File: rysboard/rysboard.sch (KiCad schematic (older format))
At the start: 8 parts, among them J1 RPi4, J17 Conn_01x03

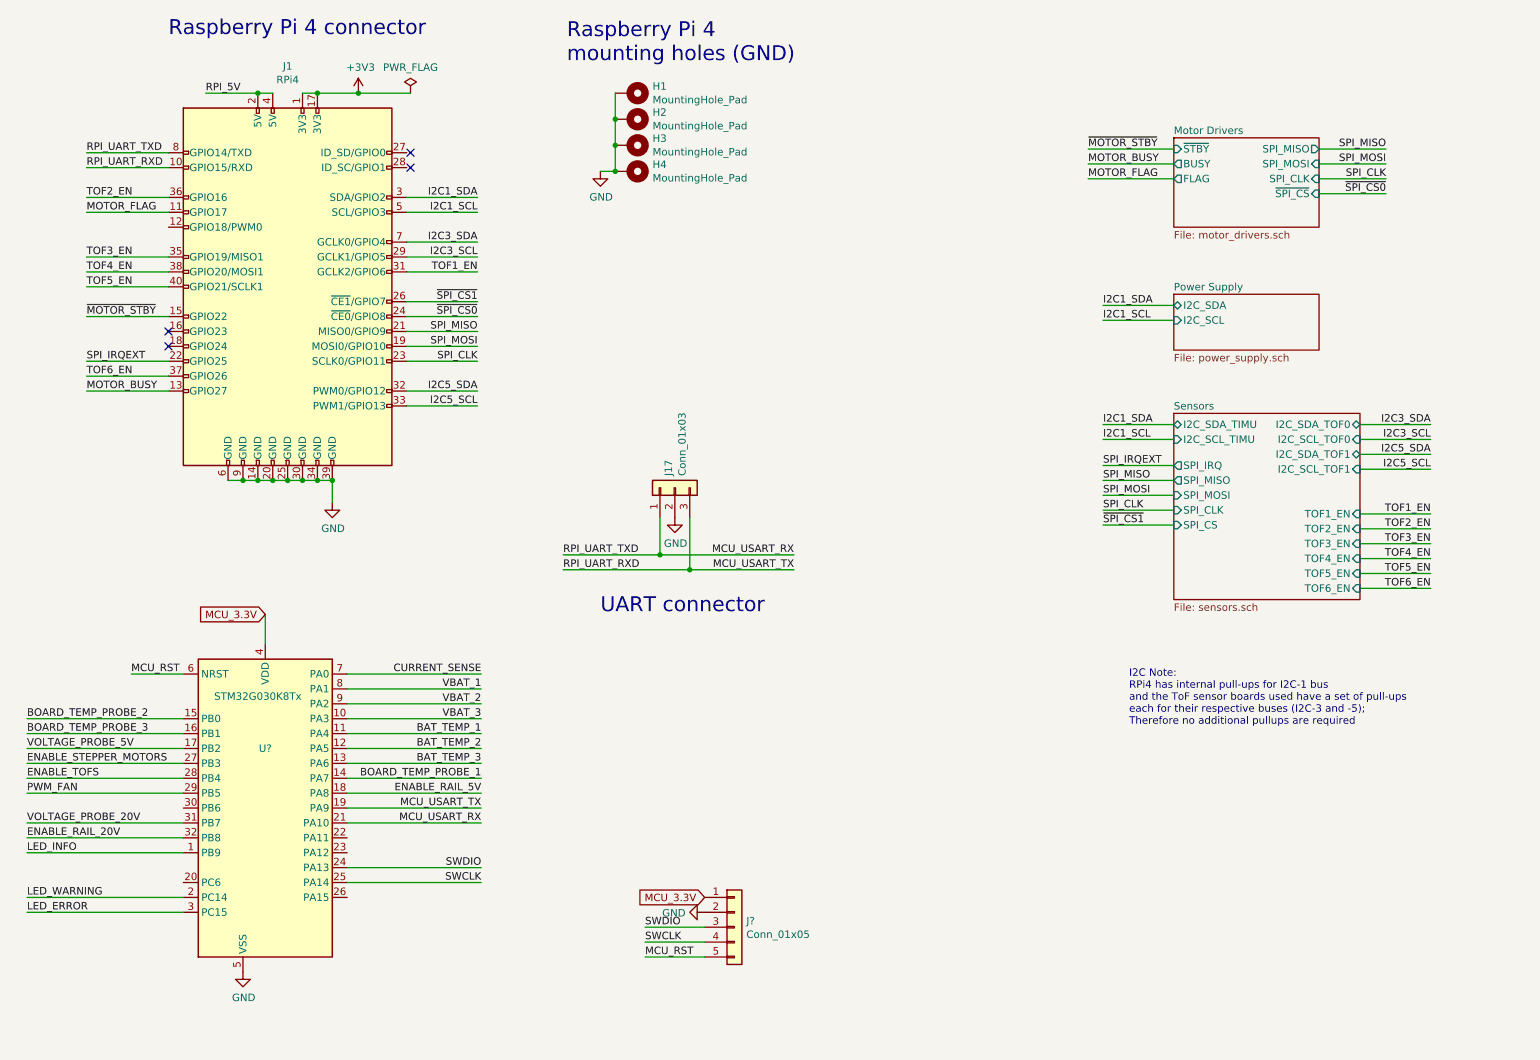
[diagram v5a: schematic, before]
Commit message: NST847BDP6T5G Added, more conections done
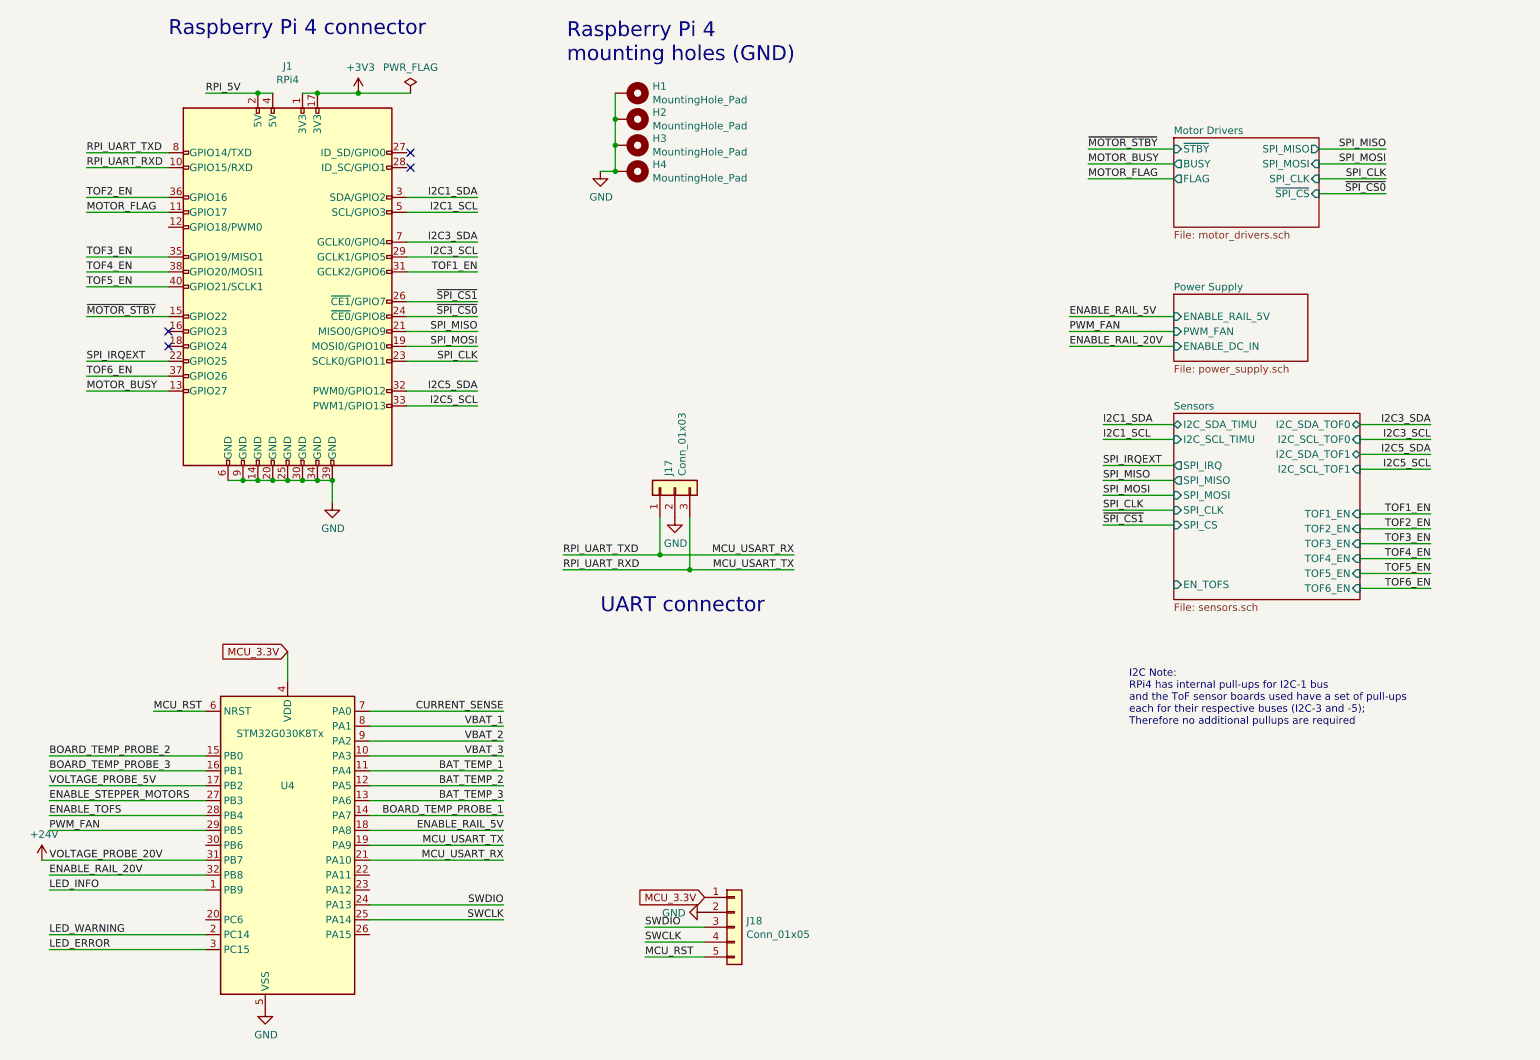
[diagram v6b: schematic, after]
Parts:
- gave numbers to parts that had none: 2
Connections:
- net VOLTAGE_PROBE_20V renamed +24V
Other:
- moved on the sheet: U4
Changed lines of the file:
@@
 $Descr A4 11693 8268
 encoding utf-8
-Sheet 1 7
+Sheet 1 6
 Title "rysboard"
 Date "2020-12-19"
@@
 Raspberry Pi 4 connector
 $Sheet
-S 8250 2550 975  375
+S 8250 2550 900  450
 U 5E8FCBC6
 F0 "Power Supply" 50
 F1 "power_supply.sch" 50
-F2 "I2C_SDA" B L 8250 2625 50
-F3 "I2C_SCL" I L 8250 2725 50
+F2 "ENABLE_RAIL_5V" I L 8250 2700 50
+F3 "PWM_FAN" I L 8250 2800 50
+F4 "ENABLE_DC_IN" I L 8250 2900 50
 $EndSheet
 Text Label 3575 2700 2    50   ~ 0
@@
 F17 "I2C_SCL_TOF1" I R 9500 3725 50
 F18 "I2C_SDA_TOF1" B R 9500 3625 50
+F19 "EN_TOFS" I L 8250 4500 50
 $EndSheet
 $Comp
@@
 Wire Wire Line
 	7775 3525 8250 3525
-Wire Wire Line
-	7775 2625 8250 2625
-Wire Wire Line
-	7775 2725 8250 2725
-Text Label 7775 2625 0    50   ~ 0
-I2C1_SDA
-Text Label 7775 2725 0    50   ~ 0
-I2C1_SCL
 Text Label 7775 3425 0    50   ~ 0
 I2C1_SDA
@@
 NoConn ~ 1500 2800
 $Comp
-L rysboard:STM32G030K8Tx U?
+L rysboard:STM32G030K8Tx U4
 U 1 1 6035F242
-P 2200 5800
-F 0 "U?" H 2150 6000 50  0000 C CNN
-F 1 "STM32G030K8Tx" H 2100 6350 50  0000 C CNN
-F 2 "Package_QFP:LQFP-32_7x7mm_P0.8mm" H 2900 4400 50  0001 R CNN
-F 3 "http://www.st.com/st-web-ui/static/active/en/resource/technical/document/datasheet/DM00088500.pdf" H 2200 5800 50  0001 C CNN
-	1    2200 5800
-	1    0    0    -1
-$EndComp
-Text GLabel 2150 4700 0    50   Input ~ 0
+P 2350 6050
+F 0 "U4" H 2300 6250 50  0000 C CNN
+F 1 "STM32G030K8Tx" H 2250 6600 50  0000 C CNN
+F 2 "Package_QFP:LQFP-32_7x7mm_P0.8mm" H 3050 4650 50  0001 R CNN
+F 3 "http://www.st.com/st-web-ui/static/active/en/resource/technical/document/datasheet/DM00088500.pdf" H 2350 6050 50  0001 C CNN
+	1    2350 6050
+	1    0    0    -1
+$EndComp
+Text GLabel 2300 4950 0    50   Input ~ 0
 MCU_3.3V
 Wire Wire Line
-	2150 4700 2150 4900
+	2300 4950 2300 5150
 Wire Wire Line
 	1900 3800 2000 3800
@@
 	2500 3800 2600 3800
 $Comp
-L power:GND #PWR?
+L power:GND #PWR02
 U 1 1 6036E13E
 P 2600 3950
-F 0 "#PWR?" H 2600 3700 50  0001 C CNN
+F 0 "#PWR02" H 2600 3700 50  0001 C CNN
 F 1 "GND" H 2605 3777 50  0000 C CNN
 F 2 "" H 2600 3950 50  0001 C CNN
@@
 	2600 3950 2600 3800
 Connection ~ 2600 3800
-Text Label 3600 6500 2    50   ~ 0
+Text Label 3750 6750 2    50   ~ 0
 SWCLK
-Text Label 3600 6400 2    50   ~ 0
+Text Label 3750 6650 2    50   ~ 0
 SWDIO
-Text Label 1250 5100 0    50   ~ 0
+Text Label 1400 5350 0    50   ~ 0
 MCU_RST
 Wire Wire Line
-	1250 5100 1600 5100
-Text Label 550  6300 0    50   ~ 0
+	1400 5350 1750 5350
+Text Label 700  6550 0    50   ~ 0
 LED_INFO
-Text Label 550  6600 0    50   ~ 0
+Text Label 700  6850 0    50   ~ 0
 LED_WARNING
-Text Label 550  6700 0    50   ~ 0
+Text Label 700  6950 0    50   ~ 0
 LED_ERROR
-Text Label 3600 5100 2    50   ~ 0
+Text Label 3750 5350 2    50   ~ 0
 CURRENT_SENSE
-Text Label 3600 5200 2    50   ~ 0
+Text Label 3750 5450 2    50   ~ 0
 VBAT_1
-Text Label 3600 5300 2    50   ~ 0
+Text Label 3750 5550 2    50   ~ 0
 VBAT_2
-Text Label 3600 5400 2    50   ~ 0
+Text Label 3750 5650 2    50   ~ 0
 VBAT_3
-Text Label 3600 5500 2    50   ~ 0
+Text Label 3750 5750 2    50   ~ 0
 BAT_TEMP_1
-Text Label 3600 5600 2    50   ~ 0
+Text Label 3750 5850 2    50   ~ 0
 BAT_TEMP_2
-Text Label 3600 5700 2    50   ~ 0
+Text Label 3750 5950 2    50   ~ 0
 BAT_TEMP_3
-Text Label 3600 5800 2    50   ~ 0
+Text Label 3750 6050 2    50   ~ 0
 BOARD_TEMP_PROBE_1
-Text Label 550  5400 0    50   ~ 0
+Text Label 700  5650 0    50   ~ 0
 BOARD_TEMP_PROBE_2
-Text Label 550  5500 0    50   ~ 0
+Text Label 700  5750 0    50   ~ 0
 BOARD_TEMP_PROBE_3
-Text Label 550  5600 0    50   ~ 0
+Text Label 700  5850 0    50   ~ 0
 VOLTAGE_PROBE_5V
-Text Label 3600 5900 2    50   ~ 0
+Text Label 3750 6150 2    50   ~ 0
 ENABLE_RAIL_5V
-Text Label 3600 6000 2    50   ~ 0
+Text Label 3750 6250 2    50   ~ 0
 MCU_USART_TX
-Text Label 3600 6100 2    50   ~ 0
+Text Label 3750 6350 2    50   ~ 0
 MCU_USART_RX
-Text Label 550  5700 0    50   ~ 0
+Text Label 700  5950 0    50   ~ 0
 ENABLE_STEPPER_MOTORS
-Text Label 550  5800 0    50   ~ 0
+Text Label 700  6050 0    50   ~ 0
 ENABLE_TOFS
-Text Label 550  5900 0    50   ~ 0
+Text Label 700  6150 0    50   ~ 0
 PWM_FAN
-Text Label 550  6100 0    50   ~ 0
+Text Label 700  6350 0    50   ~ 0
 VOLTAGE_PROBE_20V
-Text Label 550  6200 0    50   ~ 0
+Text Label 700  6450 0    50   ~ 0
 ENABLE_RAIL_20V
 Wire Wire Line
-	2700 6500 3600 6500
-Wire Wire Line
-	2700 6400 3600 6400
-Wire Wire Line
-	3600 6100 2700 6100
-Wire Wire Line
-	3600 6000 2700 6000
-Wire Wire Line
-	3600 5900 2700 5900
-Wire Wire Line
-	2700 5800 3600 5800
-Wire Wire Line
-	3600 5700 2700 5700
-Wire Wire Line
-	2700 5600 3600 5600
-Wire Wire Line
-	3600 5500 2700 5500
-Wire Wire Line
-	2700 5400 3600 5400
-Wire Wire Line
-	3600 5300 2700 5300
-Wire Wire Line
-	2700 5200 3600 5200
-Wire Wire Line
-	2700 5100 3600 5100
-Wire Wire Line
-	550  6700 1600 6700
-Wire Wire Line
-	550  6600 1600 6600
-Wire Wire Line
-	550  6300 1600 6300
-Wire Wire Line
-	550  6200 1600 6200
-Wire Wire Line
-	1600 6100 550  6100
-Wire Wire Line
-	550  5900 1600 5900
-Wire Wire Line
-	550  5800 1600 5800
-Wire Wire Line
-	1600 5700 550  5700
-Wire Wire Line
-	550  5600 1600 5600
-Wire Wire Line
-	1600 5500 550  5500
-Wire Wire Line
-	550  5400 1600 5400
-$Comp
-L power:GND #PWR?
+	2850 6750 3750 6750
+Wire Wire Line
+	2850 6650 3750 6650
+Wire Wire Line
+	3750 6350 2850 6350
+Wire Wire Line
+	3750 6250 2850 6250
+Wire Wire Line
+	3750 6150 2850 6150
+Wire Wire Line
+	2850 6050 3750 6050
+Wire Wire Line
+	3750 5950 2850 5950
+Wire Wire Line
+	2850 5850 3750 5850
+Wire Wire Line
+	3750 5750 2850 5750
+Wire Wire Line
+	2850 5650 3750 5650
+Wire Wire Line
+	3750 5550 2850 5550
+Wire Wire Line
+	2850 5450 3750 5450
+Wire Wire Line
+	2850 5350 3750 5350
+Wire Wire Line
+	700  6950 1750 6950
+Wire Wire Line
+	700  6850 1750 6850
+Wire Wire Line
+	700  6550 1750 6550
+Wire Wire Line
+	700  6450 1750 6450
+Wire Wire Line
+	700  6150 1750 6150
+Wire Wire Line
+	700  6050 1750 6050
+Wire Wire Line
+	1750 5950 700  5950
+Wire Wire Line
+	700  5850 1750 5850
+Wire Wire Line
+	1750 5750 700  5750
+Wire Wire Line
+	700  5650 1750 5650
+$Comp
+L power:GND #PWR01
 U 1 1 603FFDF1
-P 2000 7100
-F 0 "#PWR?" H 2000 6850 50  0001 C CNN
-F 1 "GND" H 2005 6927 50  0000 C CNN
-F 2 "" H 2000 7100 50  0001 C CNN
-F 3 "" H 2000 7100 50  0001 C CNN
-	1    2000 7100
-	1    0    0    -1
-$EndComp
-$Comp
-L Connector_Generic:Conn_01x05 J?
+P 2150 7350
+F 0 "#PWR01" H 2150 7100 50  0001 C CNN
+F 1 "GND" H 2155 7177 50  0000 C CNN
+F 2 "" H 2150 7350 50  0001 C CNN
+F 3 "" H 2150 7350 50  0001 C CNN
+	1    2150 7350
+	1    0    0    -1
+$EndComp
+$Comp
+L Connector_Generic:Conn_01x05 J18
 U 1 1 60400166
 P 5300 6800
-F 0 "J?" H 5380 6842 50  0000 L CNN
+F 0 "J18" H 5380 6842 50  0000 L CNN
 F 1 "Conn_01x05" H 5380 6751 50  0000 L CNN
 F 2 "Connector_PinHeader_1.00mm:PinHeader_1x05_P1.00mm_Vertical" H 5300 6800 50  0001 C CNN
@@
 MCU_RST
 $Comp
-L power:GND #PWR?
+L power:GND #PWR020
 U 1 1 60400A12
 P 5100 6700
-F 0 "#PWR?" H 5100 6450 50  0001 C CNN
+F 0 "#PWR020" H 5100 6450 50  0001 C CNN
 F 1 "GND" V 5105 6572 50  0000 R CNN
 F 2 "" H 5100 6700 50  0001 C CNN
@@
 	950  1600 1500 1600
 $Comp
-L power:GND #PWR?
+L power:GND #PWR017
 U 1 1 6046B140
 P 4900 4050
-F 0 "#PWR?" H 4900 3800 50  0001 C CNN
+F 0 "#PWR017" H 4900 3800 50  0001 C CNN
 F 1 "GND" H 4905 3877 50  0000 C CNN
 F 2 "" H 4900 4050 50  0001 C CNN
@@
 	4150 4400 5000 4400
 Connection ~ 5000 4400
+Text Label 7550 2700 0    50   ~ 0
+ENABLE_RAIL_5V
+Text Label 7550 2800 0    50   ~ 0
+PWM_FAN
+Text Label 7550 2900 0    50   ~ 0
+ENABLE_RAIL_20V
+Wire Wire Line
+	7550 2700 8250 2700
+Wire Wire Line
+	7550 2800 8250 2800
+Wire Wire Line
+	7550 2900 8250 2900
+$Comp
+L power:+24V #PWR?
+U 1 1 606D377E
+P 650 6350
+F 0 "#PWR?" H 650 6200 50  0001 C CNN
+F 1 "+24V" H 665 6523 50  0000 C CNN
+F 2 "" H 650 6350 50  0001 C CNN
+F 3 "" H 650 6350 50  0001 C CNN
+	1    650  6350
+	1    0    0    -1
+$EndComp
+Wire Wire Line
+	650  6350 1750 6350
 $EndSCHEMATC

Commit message: created eval board for STM , added mcu, created controll section for TOFS and FAN. Added programming pinout, Remooved legacy spi interface, Removed addidtional i2c socket
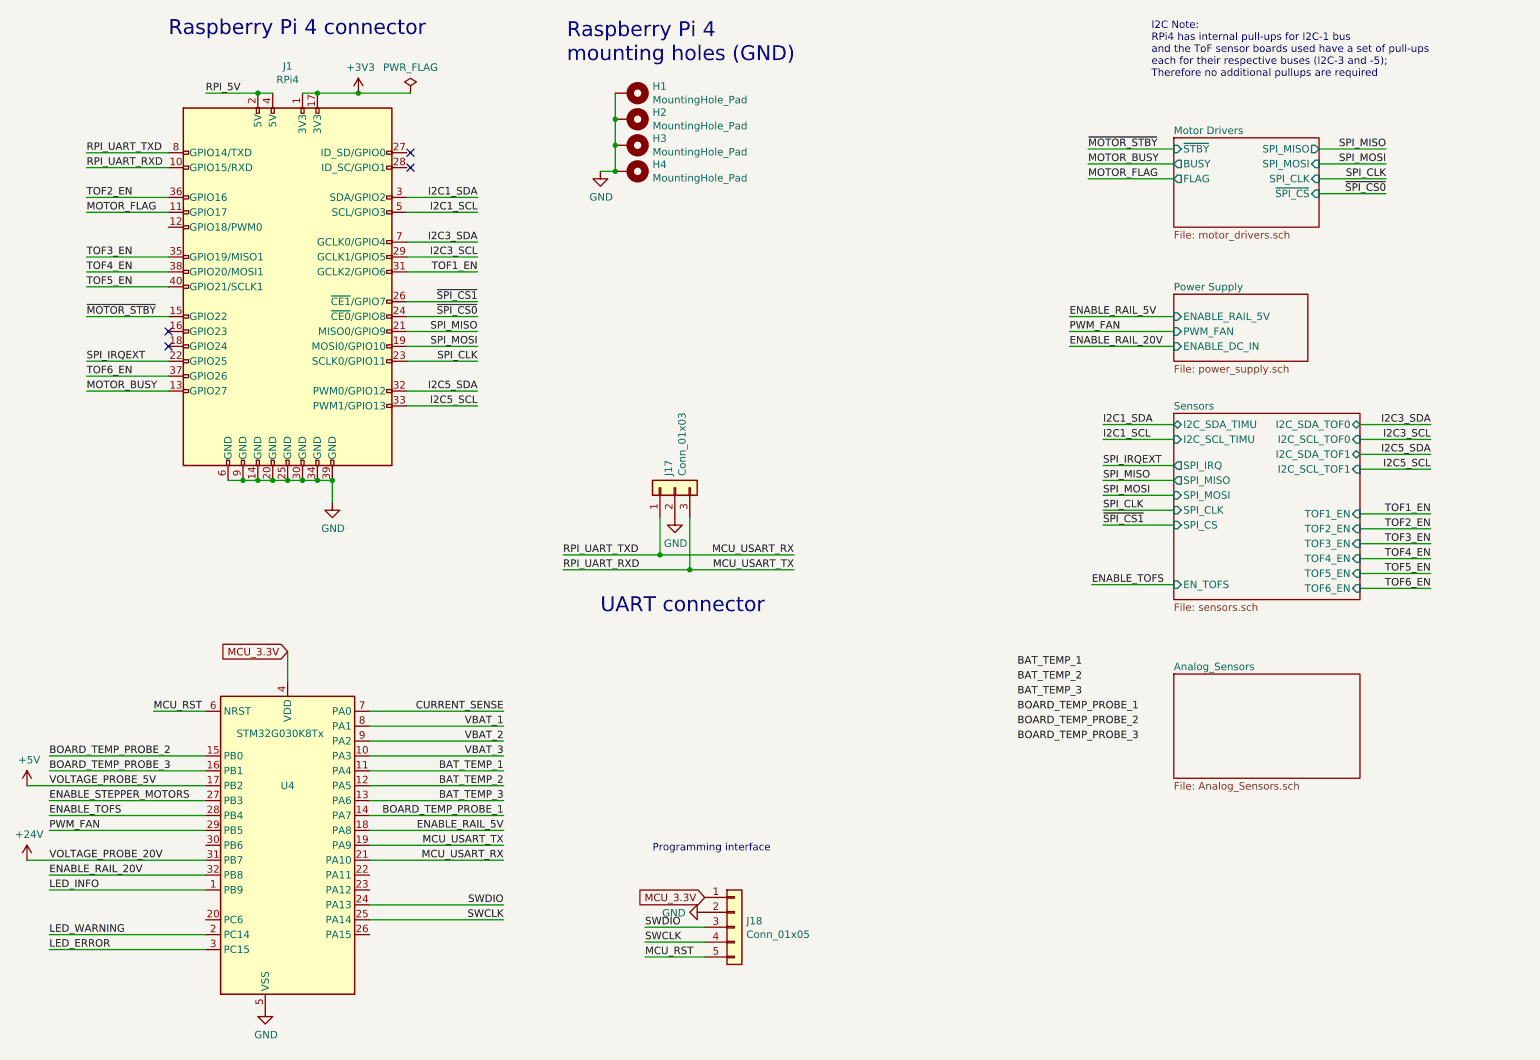
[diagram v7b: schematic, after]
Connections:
- net VOLTAGE_PROBE_5V renamed +5V
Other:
- note added: "Programming interface\n"
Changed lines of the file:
@@
 $Descr A4 11693 8268
 encoding utf-8
-Sheet 1 6
+Sheet 1 7
 Title "rysboard"
 Date "2020-12-19"
@@
 Text Notes 4175 1000 0    100  ~ 0
 Raspberry Pi 4\nmounting holes (GND)
-Text Notes 7950 5450 0    50   ~ 0
+Text Notes 8100 1100 0    50   ~ 0
 I2C Note:\nRPi4 has internal pull-ups for I2C-1 bus\nand the ToF sensor boards used have a set of pull-ups\neach for their respective buses (I2C-3 and -5);\nTherefore no additional pullups are required
 Wire Wire Line
@@
 	1750 5950 700  5950
 Wire Wire Line
-	700  5850 1750 5850
-Wire Wire Line
 	1750 5750 700  5750
 Wire Wire Line
@@
 L power:+24V #PWR?
 U 1 1 606D377E
-P 650 6350
-F 0 "#PWR?" H 650 6200 50  0001 C CNN
-F 1 "+24V" H 665 6523 50  0000 C CNN
-F 2 "" H 650 6350 50  0001 C CNN
-F 3 "" H 650 6350 50  0001 C CNN
-	1    650  6350
-	1    0    0    -1
-$EndComp
-Wire Wire Line
-	650  6350 1750 6350
+P 550 6350
+F 0 "#PWR?" H 550 6200 50  0001 C CNN
+F 1 "+24V" H 565 6523 50  0000 C CNN
+F 2 "" H 550 6350 50  0001 C CNN
+F 3 "" H 550 6350 50  0001 C CNN
+	1    550  6350
+	1    0    0    -1
+$EndComp
+Text Label 7700 4500 0    50   ~ 0
+ENABLE_TOFS
+Wire Wire Line
+	7700 4500 8250 4500
+$Sheet
+S 8250 5100 1250 700
+U 60370950
+F0 "Analog_Sensors" 50
+F1 "Analog_Sensors.sch" 50
+$EndSheet
+Text Label 7200 5450 0    50   ~ 0
+BOARD_TEMP_PROBE_2
+Text Label 7200 5550 0    50   ~ 0
+BOARD_TEMP_PROBE_3
+Text Label 7200 5350 0    50   ~ 0
+BOARD_TEMP_PROBE_1
+Text Label 7200 5250 0    50   ~ 0
+BAT_TEMP_3
+Text Label 7200 5150 0    50   ~ 0
+BAT_TEMP_2
+Text Label 7200 5050 0    50   ~ 0
+BAT_TEMP_1
+$Comp
+L power:+5V #PWR?
+U 1 1 603726EA
+P 550 5850
+F 0 "#PWR?" H 550 5700 50  0001 C CNN
+F 1 "+5V" H 565 6023 50  0000 C CNN
+F 2 "" H 550 5850 50  0001 C CNN
+F 3 "" H 550 5850 50  0001 C CNN
+	1    550  5850
+	1    0    0    -1
+$EndComp
+Wire Wire Line
+	550  5850 1750 5850
+Wire Wire Line
+	550  6350 1750 6350
+Text Notes 4750 6300 0    50   ~ 0
+Programming interface\n
 $EndSCHEMATC
